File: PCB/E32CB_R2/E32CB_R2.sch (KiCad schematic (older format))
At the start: 89 parts, among them J1 GPIO_HEADER, J10 S, J11 Q4, J12 S, J13 Q3, J14 S, J15 Q8, J16 S, J17 Q7, J18 S, J19 Q6, J2 Power, J20 S, J21 Q5, J22 S, J3 USB_B, J4 USB +5V, J5 NEXTION, J6 I2C, J7 Q1, J8 S, J9 Q2, Q1 S8050, Q10 IRLR2905, Q2 S8050, Q3 IRLR2905, Q4 IRLR2905, Q5 IRLR2905, Q6 IRLR2905, Q7 IRLR2905, Q8 IRLR2905, Q9 IRLR2905, U1 ESP32-WROOM-32, X1 12MHz

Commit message: pcb update
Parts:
- FLASH1: renamed from sw_push2; value MODE -> FLASH
- renumbered sw_push1 to RESET1
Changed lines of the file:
@@
 	3850 6950 3950 6950
 $Comp
-L Switch:SW_Push sw_push1
+L Switch:SW_Push RESET1
 U 1 1 5E140153
 P 3650 6950
-F 0 "sw_push1" H 3650 7143 50  0001 C CNN
+F 0 "RESET1" H 3650 7143 50  0001 C CNN
 F 1 "RESET" H 3650 7144 50  0000 C CNN
 F 2 "Button_Switch_THT:SW_PUSH_6mm" H 3650 7150 50  0001 C CNN
@@
 	3850 7250 3950 7250
 $Comp
-L Switch:SW_Push sw_push2
+L Switch:SW_Push FLASH1
 U 1 1 5E1870C9
 P 3650 7250
-F 0 "sw_push2" H 3650 7443 50  0001 C CNN
-F 1 "MODE" H 3650 7444 50  0000 C CNN
+F 0 "FLASH1" H 3650 7443 50  0001 C CNN
+F 1 "FLASH" H 3650 7444 50  0000 C CNN
 F 2 "Button_Switch_THT:SW_PUSH_6mm" H 3650 7450 50  0001 C CNN
 F 3 "~" H 3650 7450 50  0001 C CNN

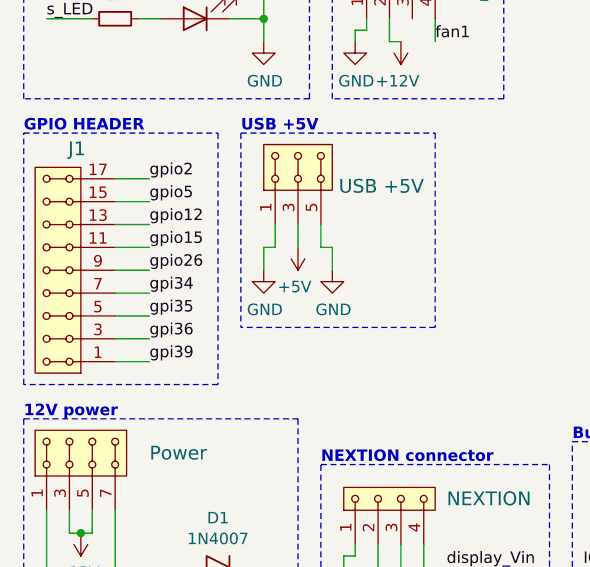
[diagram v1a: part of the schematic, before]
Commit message: gpio header pins changed
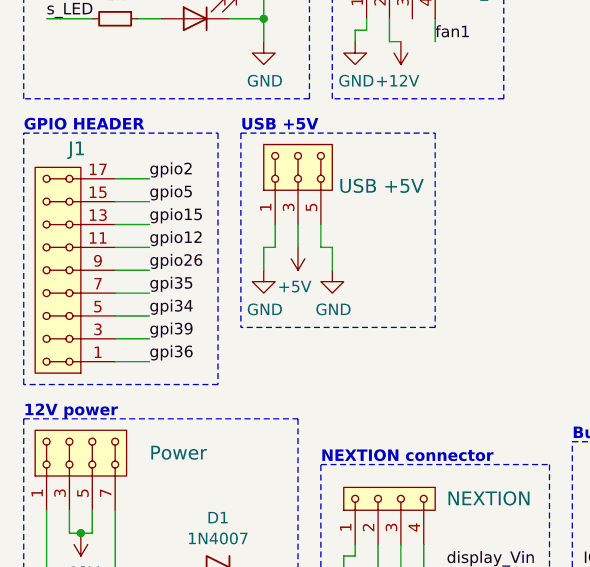
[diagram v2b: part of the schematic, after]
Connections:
- net gpi34: now also J1.5, J1.6; no longer J1.7, J1.8
- net gpi35: now also J1.7, J1.8; no longer J1.5, J1.6
- net gpi36: now also J1.1, J1.2; no longer J1.3, J1.4
- net gpi39: now also J1.3, J1.4; no longer J1.1, J1.2
- net gpio12: now also J1.11, J1.12; no longer J1.13, J1.14
- net gpio15: now also J1.13, J1.14; no longer J1.11, J1.12
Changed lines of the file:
@@
 Text Label 1300 5650 0    50   ~ 0
 gpio5
+Text Label 1300 5850 0    50   ~ 0
+gpio12
 Text Label 1300 5750 0    50   ~ 0
-gpio12
-Text Label 1300 5850 0    50   ~ 0
 gpio15
 Text Label 1300 5950 0    50   ~ 0
 gpio26
+Text Label 1300 6150 0    50   ~ 0
+gpi34
 Text Label 1300 6050 0    50   ~ 0
-gpi34
-Text Label 1300 6150 0    50   ~ 0
 gpi35
+Text Label 1300 6350 0    50   ~ 0
+gpi36
 Text Label 1300 6250 0    50   ~ 0
-gpi36
-Text Label 1300 6350 0    50   ~ 0
 gpi39
 Wire Notes Line

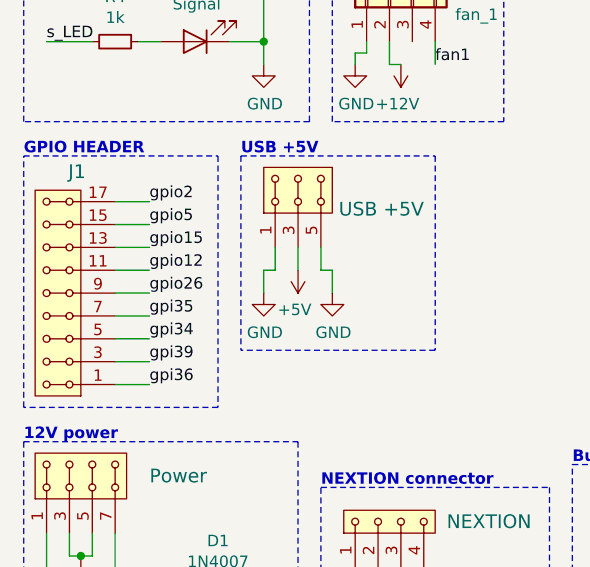
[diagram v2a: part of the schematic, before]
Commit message: gpio chenged
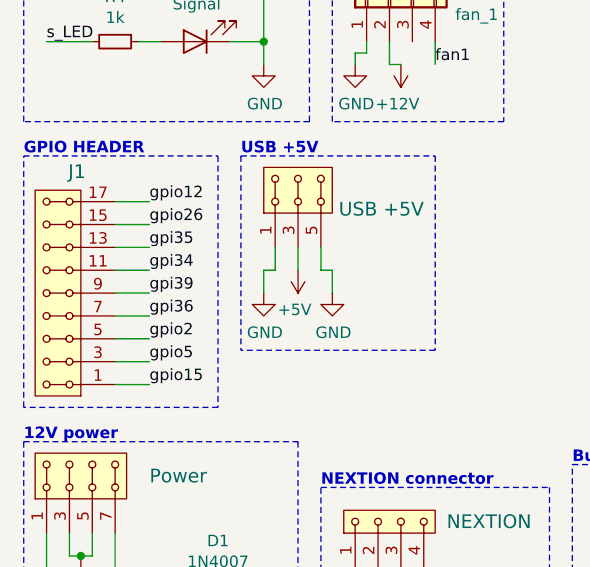
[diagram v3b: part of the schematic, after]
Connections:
- net gpi34: now also J1.11, J1.12; no longer J1.5, J1.6
- net gpi35: now also J1.13, J1.14; no longer J1.7, J1.8
- net gpi36: now also J1.7, J1.8; no longer J1.1, J1.2
- net gpi39: now also J1.10, J1.9; no longer J1.3, J1.4
- net gpio12: now also J1.17, J1.18; no longer J1.11, J1.12
- net gpio15: now also J1.1, J1.2; no longer J1.13, J1.14
- net gpio2: now also J1.5, J1.6; no longer J1.17, J1.18
- net gpio26: now also J1.15, J1.16; no longer J1.10, J1.9
- net gpio5: now also J1.3, J1.4; no longer J1.15, J1.16
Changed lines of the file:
@@
 $EndComp
+Wire Wire Line
+	1150 6150 1300 6150
+Wire Wire Line
+	1150 6250 1300 6250
+Wire Wire Line
+	1150 6350 1300 6350
 Wire Wire Line
 	1150 5550 1300 5550
@@
 Wire Wire Line
 	1150 6050 1300 6050
-Wire Wire Line
-	1150 6150 1300 6150
-Wire Wire Line
-	1150 6250 1300 6250
-Wire Wire Line
-	1150 6350 1300 6350
+Text Label 1300 6150 0    50   ~ 0
+gpio2
+Text Label 1300 6250 0    50   ~ 0
+gpio5
 Text Label 1300 5550 0    50   ~ 0
-gpio2
+gpio12
+Text Label 1300 6350 0    50   ~ 0
+gpio15
 Text Label 1300 5650 0    50   ~ 0
-gpio5
+gpio26
 Text Label 1300 5850 0    50   ~ 0
-gpio12
+gpi34
 Text Label 1300 5750 0    50   ~ 0
-gpio15
+gpi35
+Text Label 1300 6050 0    50   ~ 0
+gpi36
 Text Label 1300 5950 0    50   ~ 0
-gpio26
-Text Label 1300 6150 0    50   ~ 0
-gpi34
-Text Label 1300 6050 0    50   ~ 0
-gpi35
-Text Label 1300 6350 0    50   ~ 0
-gpi36
-Text Label 1300 6250 0    50   ~ 0
 gpi39
 Wire Notes Line

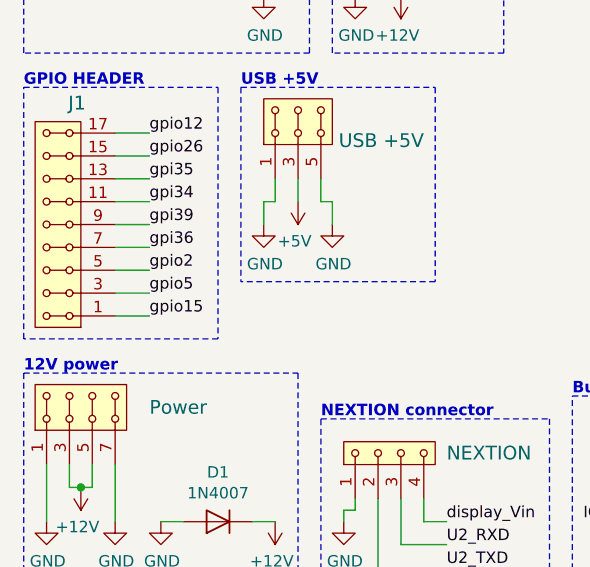
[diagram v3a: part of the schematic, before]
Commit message: gpio connected
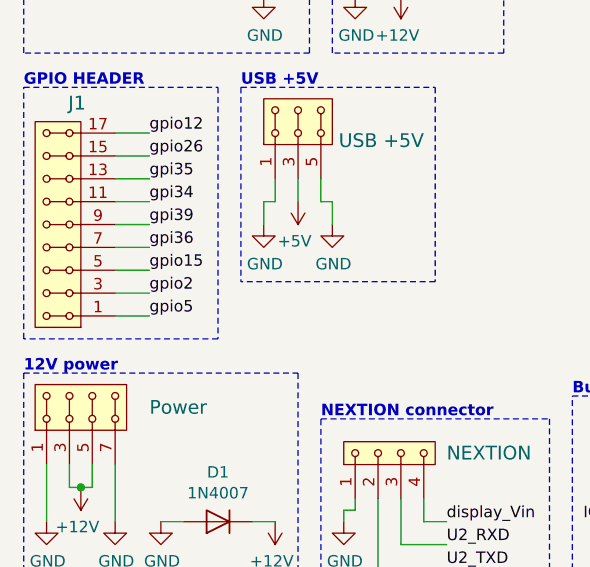
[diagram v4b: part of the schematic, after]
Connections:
- net gpio15: now also J1.5, J1.6; no longer J1.1, J1.2
- net gpio2: now also J1.3, J1.4; no longer J1.5, J1.6
- net gpio5: now also J1.1, J1.2; no longer J1.3, J1.4
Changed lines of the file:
@@
 Wire Wire Line
 	1150 6050 1300 6050
-Text Label 1300 6150 0    50   ~ 0
+Text Label 1300 6250 0    50   ~ 0
 gpio2
-Text Label 1300 6250 0    50   ~ 0
+Text Label 1300 6350 0    50   ~ 0
 gpio5
 Text Label 1300 5550 0    50   ~ 0
 gpio12
-Text Label 1300 6350 0    50   ~ 0
+Text Label 1300 6150 0    50   ~ 0
 gpio15
 Text Label 1300 5650 0    50   ~ 0

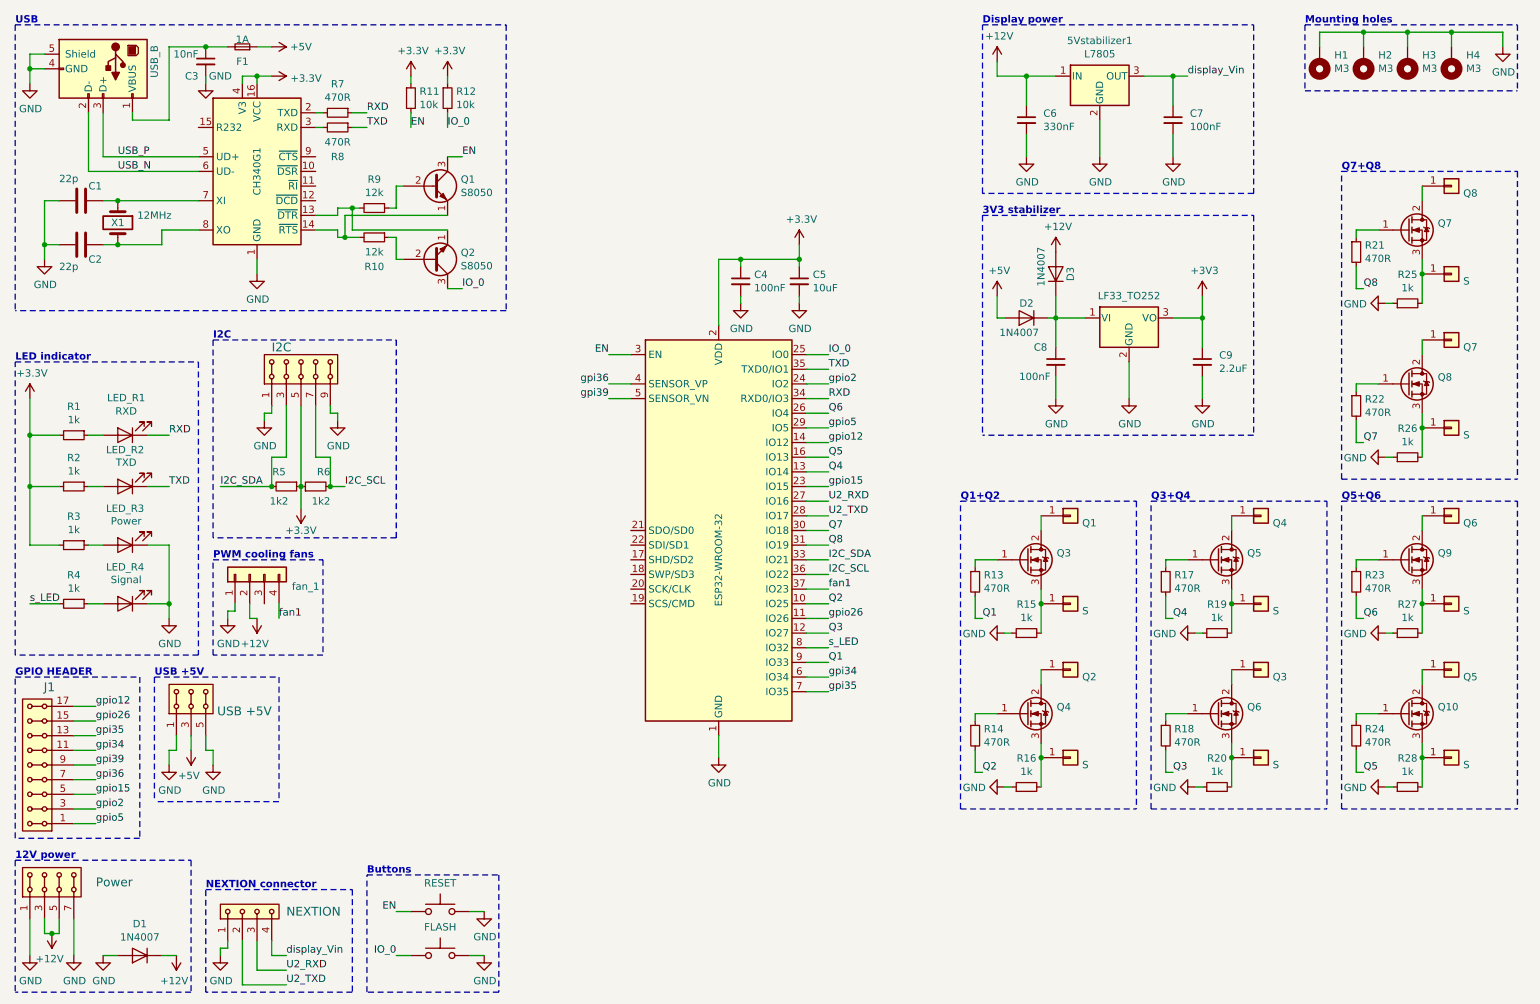
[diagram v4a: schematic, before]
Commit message: MOSFET driving
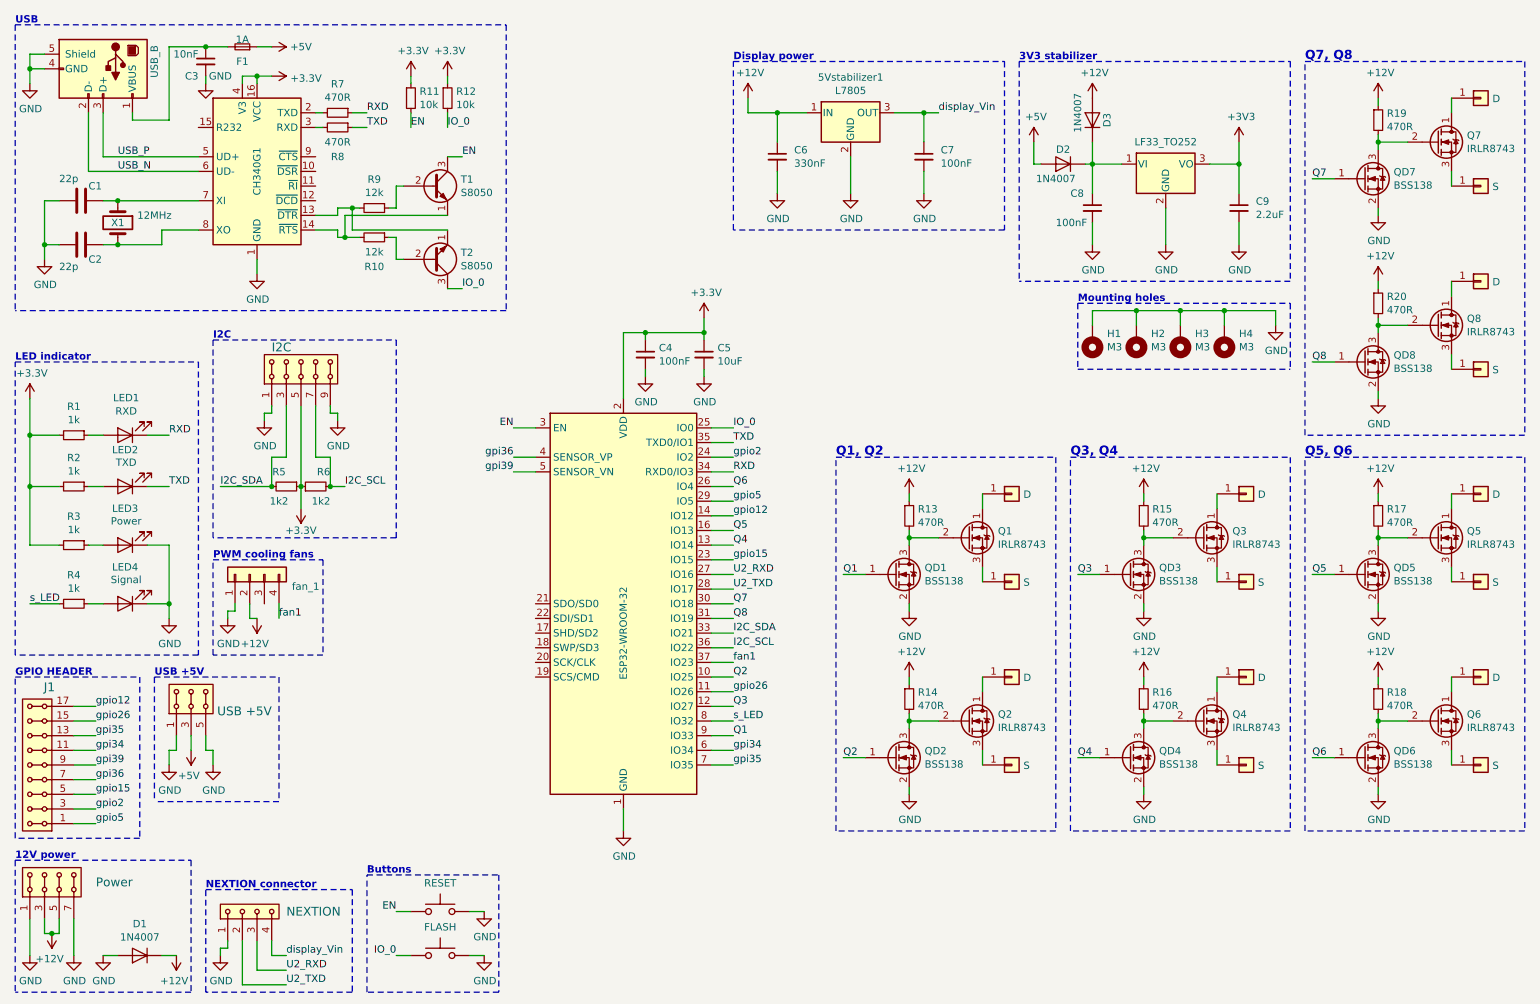
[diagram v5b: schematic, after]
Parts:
- removed Q10, Q3, Q4, Q5, Q6, Q7, Q8, Q9: IRLR2905, Package_TO_SOT_SMD:TO-252-2, symbol Transistor_FET:IRLZ44N
- removed R21, R22, R23, R24: 470R, Resistor_SMD:R_0805_2012Metric_Pad1.15x1.40mm_HandSolder, symbol Device:R_Small
- removed R25, R26, R27, R28: 1k, Resistor_SMD:R_0805_2012Metric_Pad1.15x1.40mm_HandSolder, symbol Device:R_Small
- added Q1, Q2, Q3, Q4, Q5, Q6, Q7, Q8: IRLR8743, Package_TO_SOT_SMD:TO-252-2_TabPin1, symbol Transistor_FET:IRF8308M
- added QD1, QD2, QD3, QD4, QD5, QD6, QD7, QD8: BSS138, Package_TO_SOT_SMD:SOT-23, symbol Transistor_FET:BSS138
- 3V3stabilizer1, 5Vstabilizer1: footprint Package_TO_SOT_SMD:TO-252-2 -> Package_TO_SOT_SMD:TO-252-2_TabPin1
- J11: value Q4 -> D
- J13: value Q3 -> D
- J15: value Q8 -> D
- J17: value Q7 -> D
- J19: value Q6 -> D
- J21: value Q5 -> D
- J7: value Q1 -> D
- J9: value Q2 -> D
- R15, R16, R19, R20: value 1k -> 470R
- renumbered LED_R1 to LED1, LED_R2 to LED2, LED_R3 to LED3, LED_R4 to LED4, RESET1 to S1, FLASH1 to S2, Q1 to T1, Q2 to T2
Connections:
- net +12V: now also R13.1, R14.1, R15.1, R16.1, R17.1, R18.1, R19.1, R20.1
- net GND: now also QD1.2 (S), QD2.2 (S), QD3.2 (S), QD4.2 (S), QD5.2 (S), QD6.2 (S), QD7.2 (S), QD8.2 (S); no longer R15.1, R16.1, R19.1, R20.1
- net Q1: now also QD1.1 (G); no longer R13.2
- net Q2: now also QD2.1 (G); no longer R14.2
- net Q3: now also QD3.1 (G); no longer R18.2
- net Q4: now also QD4.1 (G); no longer R17.2
- net Q5: now also QD5.1 (G)
- net Q6: now also QD6.1 (G)
- net Q7: now also QD7.1 (G)
- net Q8: now also QD8.1 (G)
- net at J7.1 (Pin_1): now also Q1.1 (D)
- net at J8.1 (Pin_1): now also Q1.3 (S); no longer R15.2
- net at J9.1 (Pin_1): now also Q2.1 (D)
- net at J10.1 (Pin_1): now also Q2.3 (S); no longer R16.2
- net at J15.1 (Pin_1): now also Q7.1 (D)
- net at J16.1 (Pin_1): now also Q7.3 (S)
- net at J17.1 (Pin_1): now also Q8.1 (D)
- net at J18.1 (Pin_1): now also Q8.3 (S)
- net at J19.1 (Pin_1): now also Q5.1 (D)
- net at J20.1 (Pin_1): now also Q5.3 (S)
- net at J21.1 (Pin_1): now also Q6.1 (D)
- net at J22.1 (Pin_1): now also Q6.3 (S)
- net at J11.1 (Pin_1): now also Q3.1 (D)
- net at J12.1 (Pin_1): now also Q3.3 (S); no longer R19.2
- net at J13.1 (Pin_1): now also Q4.1 (D)
- net at J14.1 (Pin_1): now also Q4.3 (S); no longer R20.2
- new net: Q1.2 (G), QD1.3 (D), R13.2
- new net: Q2.2 (G), QD2.3 (D), R14.2
- new net: Q3.2 (G), QD3.3 (D), R15.2
- new net: Q4.2 (G), QD4.3 (D), R16.2
- new net: Q5.2 (G), QD5.3 (D), R17.2
- new net: Q6.2 (G), QD6.3 (D), R18.2
- new net: Q7.2 (G), QD7.3 (D), R19.2
- new net: Q8.2 (G), QD8.3 (D), R20.2
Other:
- note added: "Q1, Q2"
- note added: "Q3, Q4"
- note added: "Q5, Q6"
- note added: "Q7, Q8"
- note removed: "Q1+Q2"
- note removed: "Q3+Q4"
- note removed: "Q5+Q6"
- note removed: "Q7+Q8"
- moved on the sheet: 5Vstabilizer1, C4, C5, C6, C7, C8, C9, D2, D3, H1, H2, H3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

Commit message: PCB refresh
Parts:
- 3V3stabilizer1, 5Vstabilizer1, Q1, Q2, Q3, Q4, Q5, Q6, Q7, Q8: footprint Package_TO_SOT_SMD:TO-252-2_TabPin1 -> Package_TO_SOT_SMD:TO-252-2
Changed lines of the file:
@@
 F 0 "3V3stabilizer1" H 8600 2092 50  0001 C CNN
 F 1 "LF33_TO252" H 8600 2001 50  0000 C CNN
-F 2 "Package_TO_SOT_SMD:TO-252-2_TabPin1" H 8600 2075 50  0001 C CIN
+F 2 "Package_TO_SOT_SMD:TO-252-2" H 8600 2075 50  0001 C CIN
 F 3 "http://www.st.com/content/ccc/resource/technical/document/datasheet/c4/0e/7e/2a/be/bc/4c/bd/CD00000546.pdf/files/CD00000546.pdf/jcr:content/translations/en.CD00000546.pdf" H 8600 1800 50  0001 C CNN
 	1    8600 1850
@@
 F 0 "5Vstabilizer1" H 6450 1742 50  0000 C CNN
 F 1 "L7805" H 6450 1651 50  0000 C CNN
-F 2 "Package_TO_SOT_SMD:TO-252-2_TabPin1" H 6475 1350 50  0001 L CIN
+F 2 "Package_TO_SOT_SMD:TO-252-2" H 6475 1350 50  0001 L CIN
 F 3 "http://www.st.com/content/ccc/resource/technical/document/datasheet/41/4f/b3/b0/12/d4/47/88/CD00000444.pdf/files/CD00000444.pdf/jcr:content/translations/en.CD00000444.pdf" H 6450 1450 50  0001 C CNN
 	1    6450 1500
@@
 F 0 "Q1" H 7455 4446 50  0000 L CNN
 F 1 "IRLR8743" H 7455 4355 50  0000 L CNN
-F 2 "Package_TO_SOT_SMD:TO-252-2_TabPin1" H 7250 4400 50  0001 C CIN
+F 2 "Package_TO_SOT_SMD:TO-252-2" H 7250 4400 50  0001 C CIN
 F 3 "https://www.infineon.com/dgdl/irf8308mpbf.pdf?fileId=5546d462533600a40153560d319d1d61" H 7250 4400 50  0001 L CNN
 	1    7250 4400
@@
 F 0 "Q2" H 7455 5696 50  0000 L CNN
 F 1 "IRLR8743" H 7455 5605 50  0000 L CNN
-F 2 "Package_TO_SOT_SMD:TO-252-2_TabPin1" H 7250 5650 50  0001 C CIN
+F 2 "Package_TO_SOT_SMD:TO-252-2" H 7250 5650 50  0001 C CIN
 F 3 "https://www.infineon.com/dgdl/irf8308mpbf.pdf?fileId=5546d462533600a40153560d319d1d61" H 7250 5650 50  0001 L CNN
 	1    7250 5650
@@
 F 0 "Q3" H 9055 4446 50  0000 L CNN
 F 1 "IRLR8743" H 9055 4355 50  0000 L CNN
-F 2 "Package_TO_SOT_SMD:TO-252-2_TabPin1" H 8850 4400 50  0001 C CIN
+F 2 "Package_TO_SOT_SMD:TO-252-2" H 8850 4400 50  0001 C CIN
 F 3 "https://www.infineon.com/dgdl/irf8308mpbf.pdf?fileId=5546d462533600a40153560d319d1d61" H 8850 4400 50  0001 L CNN
 	1    8850 4400
@@
 F 0 "Q4" H 9055 5696 50  0000 L CNN
 F 1 "IRLR8743" H 9055 5605 50  0000 L CNN
-F 2 "Package_TO_SOT_SMD:TO-252-2_TabPin1" H 8850 5650 50  0001 C CIN
+F 2 "Package_TO_SOT_SMD:TO-252-2" H 8850 5650 50  0001 C CIN
 F 3 "https://www.infineon.com/dgdl/irf8308mpbf.pdf?fileId=5546d462533600a40153560d319d1d61" H 8850 5650 50  0001 L CNN
 	1    8850 5650
@@
 F 0 "Q5" H 10655 4446 50  0000 L CNN
 F 1 "IRLR8743" H 10655 4355 50  0000 L CNN
-F 2 "Package_TO_SOT_SMD:TO-252-2_TabPin1" H 10450 4400 50  0001 C CIN
+F 2 "Package_TO_SOT_SMD:TO-252-2" H 10450 4400 50  0001 C CIN
 F 3 "https://www.infineon.com/dgdl/irf8308mpbf.pdf?fileId=5546d462533600a40153560d319d1d61" H 10450 4400 50  0001 L CNN
 	1    10450 4400
@@
 F 0 "Q6" H 10655 5696 50  0000 L CNN
 F 1 "IRLR8743" H 10655 5605 50  0000 L CNN
-F 2 "Package_TO_SOT_SMD:TO-252-2_TabPin1" H 10450 5650 50  0001 C CIN
+F 2 "Package_TO_SOT_SMD:TO-252-2" H 10450 5650 50  0001 C CIN
 F 3 "https://www.infineon.com/dgdl/irf8308mpbf.pdf?fileId=5546d462533600a40153560d319d1d61" H 10450 5650 50  0001 L CNN
 	1    10450 5650
@@
 F 0 "Q7" H 10655 1746 50  0000 L CNN
 F 1 "IRLR8743" H 10655 1655 50  0000 L CNN
-F 2 "Package_TO_SOT_SMD:TO-252-2_TabPin1" H 10450 1700 50  0001 C CIN
+F 2 "Package_TO_SOT_SMD:TO-252-2" H 10450 1700 50  0001 C CIN
 F 3 "https://www.infineon.com/dgdl/irf8308mpbf.pdf?fileId=5546d462533600a40153560d319d1d61" H 10450 1700 50  0001 L CNN
 	1    10450 1700
@@
 F 0 "Q8" H 10655 2996 50  0000 L CNN
 F 1 "IRLR8743" H 10655 2905 50  0000 L CNN
-F 2 "Package_TO_SOT_SMD:TO-252-2_TabPin1" H 10450 2950 50  0001 C CIN
+F 2 "Package_TO_SOT_SMD:TO-252-2" H 10450 2950 50  0001 C CIN
 F 3 "https://www.infineon.com/dgdl/irf8308mpbf.pdf?fileId=5546d462533600a40153560d319d1d61" H 10450 2950 50  0001 L CNN
 	1    10450 2950
